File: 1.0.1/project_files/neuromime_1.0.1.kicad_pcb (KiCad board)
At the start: 2 copper layers, 56 x 56 mm, 57 parts, among them K1 inhibit, K2 excite, K3 excite, K4 excite, P1 mnt, P2 axon, P3 axon, P4 axon, P5 long, U1 LM311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

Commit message: work on 1.0.1 board; autoroute test
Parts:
- removed C2, C3: 0.1uF, Capacitor_THT:C_Disc_D3.0mm_W1.6mm_P2.50mm
- moved C1 56.2 mm to (145.1, 69.2)
- moved D5 42.5 mm to (130.9, 60.2), turned to 180 degrees
- moved W3 33.2 mm to (135.4, 60.2)
- moved R8 7.59 mm to (158.3, 36.9), turned to 0 degrees
- moved R10 5.43 mm to (165.4, 63.2)
- moved R12 4.93 mm to (157.0, 63.2)
- moved C11 3.73 mm to (135.9, 67.4)
- moved W1 2.70 mm to (158.3, 27.1), turned to 68 degrees
- moved R15 2.29 mm to (172.0, 46.8), turned to 180 degrees
- moved R13 2.27 mm to (138.2, 70.1)
- moved R9 2.13 mm to (171.7, 43.6)
- moved R5 2.07 mm to (133.6, 37.6), turned to 270 degrees
- moved C10 1.91 mm to (160.0, 62.8)
- moved R11 1.78 mm to (141.9, 70.9)
- moved R7 1.72 mm to (163.8, 34.3), turned to 270 degrees
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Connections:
- C14 pad 1: GND -> Net-(C14-Pad1)
- C14 pad 2: Net-(C14-Pad2) -> GND
- R14 pad 1: Net-(C14-Pad2) -> Net-(C14-Pad1)
- U3 pad 6: Net-(C14-Pad2) -> Net-(C14-Pad1)
- U3 pad 7: Net-(C14-Pad2) -> Net-(C14-Pad1)
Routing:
- net VCC: track 0.00 -> 231.1 mm
- net GND: track 0.00 -> 220.7 mm
- net refractory: track 0.00 -> 76.2 mm
- net Net-(P2-Pad2): track 0.00 -> 60.7 mm
- net Net-(C10-Pad2): track 0.00 -> 51.6 mm
- net Net-(C5-Pad1): track 0.00 -> 43.0 mm
- net Net-(P5-Pad2): track 0.00 -> 23.6 mm
- net Net-(D2-Pad1): track 0.00 -> 18.6 mm
- net Net-(D3-Pad1): track 0.00 -> 18.4 mm
- net Net-(C8-Pad1): track 0.00 -> 15.2 mm
- net Net-(C14-Pad1): track 0.00 -> 13.9 mm
- net Net-(C11-Pad1): track 0.00 -> 13.4 mm
- net Net-(C10-Pad1): track 0.00 -> 12.0 mm
- net Net-(C6-Pad2): track 0.00 -> 11.4 mm
- net Net-(C17-Pad1): track 0.00 -> 11.1 mm
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
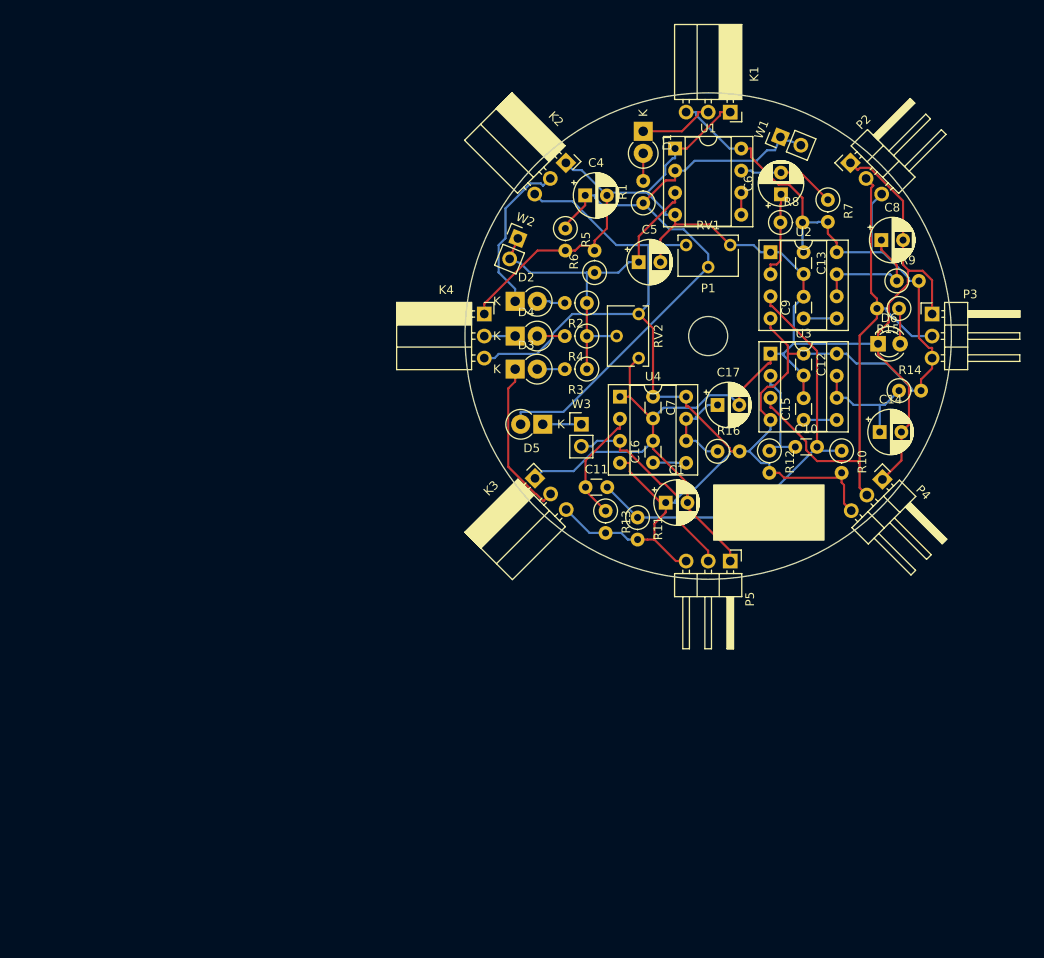
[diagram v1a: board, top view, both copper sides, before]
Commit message: work on 1.0.1; increase autoroute spacing to .5mm; labelling
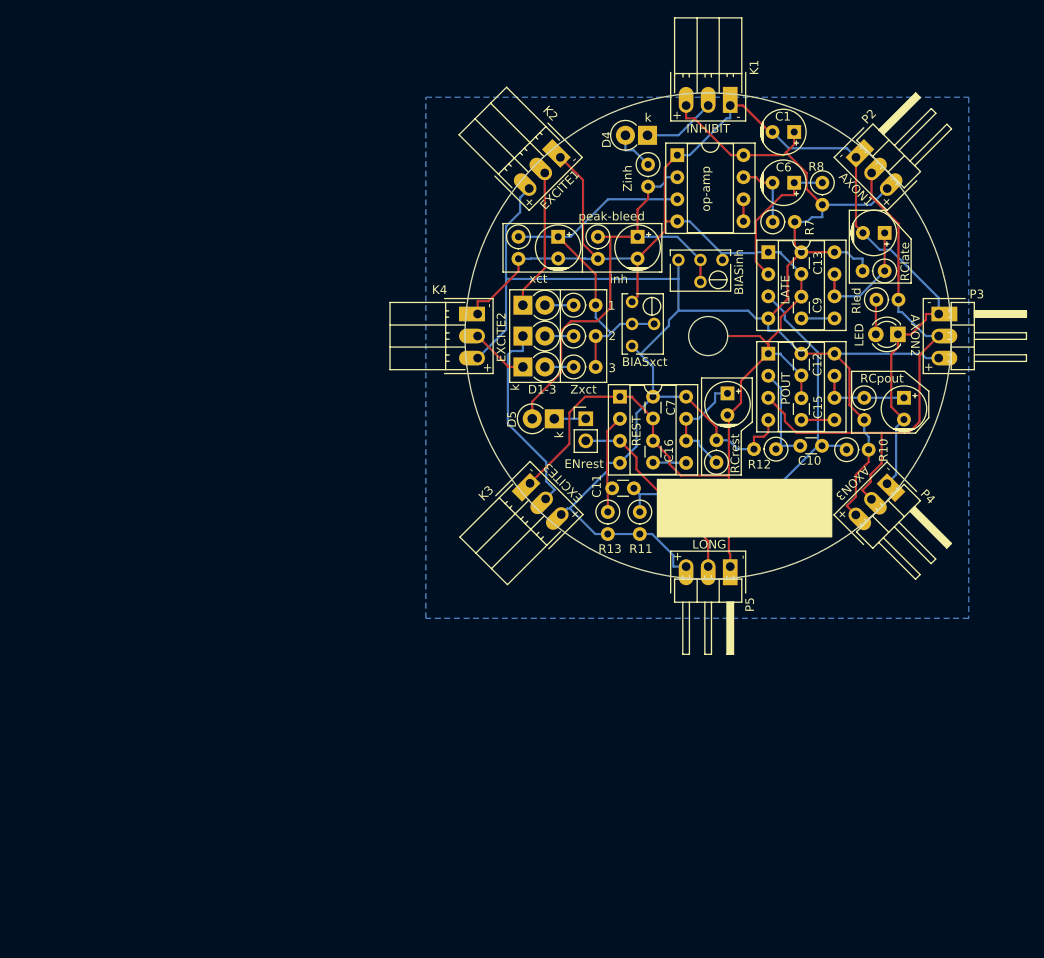
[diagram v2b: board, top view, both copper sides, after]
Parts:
- removed W1: TSTinh, Connector_PinHeader_2.54mm:PinHeader_1x02_P2.54mm_Vertical
- removed W2: TSTxct, Connector_PinHeader_2.54mm:PinHeader_1x02_P2.54mm_Vertical
- C1, C14, C17, C4, C5, C6, C8: footprint Capacitor_THT:CP_Radial_D5.0mm_P2.50mm -> flemming_feetprint_2016:CP_Radial_D5.0mm_P2.50mm_positive_symbol_inside
- K1, K2, K3, K4: footprint Connector_PinSocket_2.54mm:PinSocket_1x03_P2.54mm_Horizontal -> flemming_feetprint_2016:PinSocket_1x03_P2.54mm_Horizontal_elongated
- P2, P3, P4, P5: footprint Connector_PinHeader_2.54mm:PinHeader_1x03_P2.54mm_Horizontal -> flemming_feetprint_2016:PinHeader_1x03_P2.54mm_Horizontal_elomgated_pads
- R1: value Zinh -> Zxct; footprint Resistor_THT:R_Axial_DIN0207_L6.3mm_D2.5mm_P2.54mm_Vertical -> flemming_feetprint_2016:R_Axial_DIN0207_L6.3mm_D2.5mm_P2.54mm_Vertical_pad_numbers_reversed
- R2, R3: footprint Resistor_THT:R_Axial_DIN0207_L6.3mm_D2.5mm_P2.54mm_Vertical -> flemming_feetprint_2016:R_Axial_DIN0207_L6.3mm_D2.5mm_P2.54mm_Vertical_pad_numbers_reversed
- R4: value Zxct -> Zinh; footprint Resistor_THT:R_Axial_DIN0207_L6.3mm_D2.5mm_P2.54mm_Vertical -> flemming_feetprint_2016:R_Axial_DIN0207_L6.3mm_D2.5mm_P2.54mm_Vertical_pad_numbers_reversed
- RV1, RV2: footprint Potentiometer_THT:Potentiometer_Bourns_3266W_Vertical -> flemming_feetprint_2016:Potentiometer_Bourns_3266W_Vertical_pin_variation
- moved C1 45.2 mm to (159.9, 26.5), turned to 180 degrees
- moved D4 27.7 mm to (143.0, 26.9), turned to 180 degrees
- moved D1 24.3 mm to (128.7, 46.4), turned to 0 degrees
- moved R4 21.0 mm to (143.1, 30.3), turned to 270 degrees
- moved R1 14.2 mm to (134.5, 46.4), turned to 0 degrees
- moved C5 9.72 mm to (132.7, 38.6), turned to 270 degrees
- moved R6 9.69 mm to (128.2, 38.6), turned to 270 degrees
- moved C4 7.69 mm to (141.9, 38.6), turned to 270 degrees
- moved R7 6.84 mm to (157.4, 36.9), turned to 0 degrees
- moved R8 6.65 mm to (163.1, 32.3), turned to 270 degrees
- moved RV2 6.52 mm to (141.2, 46.1), turned to 90 degrees
- moved C14 4.83 mm to (172.5, 57.1), turned to 270 degrees
- moved R2 4.10 mm to (134.5, 50.0), turned to 0 degrees
- moved D2 4.10 mm to (128.7, 50.0)
- moved R14 4.09 mm to (168.0, 57.1), turned to 270 degrees
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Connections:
- K1 pad 2: Net-(D1-Pad1) -> Net-(D4-Pad1)
- K2 pad 2: Net-(D2-Pad1) -> Net-(D1-Pad1)
- K3 pad 2: Net-(D3-Pad1) -> Net-(D2-Pad1)
- K4 pad 2: Net-(D4-Pad1) -> Net-(D3-Pad1)
- R1 pad 1: refractory -> Net-(C5-Pad1)
- R4 pad 1: Net-(C5-Pad1) -> refractory
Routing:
- net refractory: track 76.2 -> 52.3 mm
- net GND: track 220.7 -> 236.7 mm
- net Net-(D3-Pad1): track 18.4 -> 6.72 mm
- net Net-(D1-Pad1): track 8.61 -> 16.3 mm
- net Net-(C6-Pad1): track 10.1 -> 17.0 mm
- net Net-(D4-Pad1): track 3.56 -> 8.41 mm
- net Net-(D2-Pad1): track 18.6 -> 22.9 mm
- net Net-(C14-Pad1): track 13.9 -> 10.5 mm
- net Net-(C6-Pad2): track 11.4 -> 8.12 mm
- net Net-(C17-Pad1): track 11.1 -> 13.9 mm
- net Net-(C10-Pad2): track 51.6 -> 48.9 mm
- net Net-(P2-Pad2): track 60.7 -> 62.9 mm
- net Net-(D4-Pad2): track 3.18 -> 5.01 mm
- net Net-(C11-Pad1): track 13.4 -> 11.8 mm
- net Net-(C5-Pad1): track 43.0 -> 44.5 mm
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- added copper zone on B.Cu, net GND
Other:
- board text added: "1"
- board text added: "2"
- board text added: "3"
- board text added: "AXON1"
- board text added: "AXON2"
- board text added: "AXON3"
- board text added: "BIASinh"
- board text added: "BIASxct"
- board text added: "C12"
- board text added: "C13"
- board text added: "C15"
- board text added: "C16"
- board text added: "C7"
- board text added: "C9"
- board text added: "D1-3"
- board text added: "ENrest"
- board text added: "EXCITE1"
- board text added: "EXCITE2"
- board text added: "EXCITE3"
- board text added: "INHIBIT"
- board text added: "LATE"
- board text added: "LED"
- board text added: "LONG"
- board text added: "Norman White's Neuromime version 1.0.1 July 2019, Berlin github.com/gnimm/neuromime"
- board text added: "POUT"
- board text added: "RClate"
- board text added: "RCpout"
- board text added: "RCrest"
- board text added: "REST"
- board text added: "Rled"
- board text added: "Zinh"
- board text added: "Zxct"
- board text added: "inh"
- board text added: "k"
- board text added: "op-amp"
- board text added: "peak-bleed"
- board text added: "xct"

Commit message: work on 1.0.1;housekeeping; paths; included footprints libs
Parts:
- P1: footprint MountingHole:MountingHole_4.5mm -> flemming_feetprint_2019:MountingHole_4.5mm_PTH
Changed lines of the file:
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@@
   (page A4)
   (layers
-    (0 F.Cu signal hide)
+    (0 F.Cu signal)
     (31 B.Cu signal hide)
-    (32 B.Adhes user)
+    (32 B.Adhes user hide)
     (33 F.Adhes user)
-    (34 B.Paste user)
-    (35 F.Paste user)
+    (34 B.Paste user hide)
+    (35 F.Paste user hide)
     (36 B.SilkS user)
     (37 F.SilkS user)
@@
     (46 B.CrtYd user)
     (47 F.CrtYd user)
-    (48 B.Fab user)
+    (48 B.Fab user hide)
     (49 F.Fab user hide)
   )
@@
     )
   )
-  (module MountingHole:MountingHole_4.5mm (layer F.Cu)
-    (at 150 50)
-    (descr "Mounting Hole 4.5mm, no annular")
-    (tags "mounting hole 4.5mm no annular")
-    (attr virtual)
-    (fp_text reference P1 (at 0 -5.5) (layer F.SilkS) hide
-      (effects (font (size 1 1) (thickness 0.15)))
-    )
-    (fp_text value mnt (at 0 5.5) (layer F.Fab) hide
-      (effects (font (size 1 1) (thickness 0.15)))
-    )
-    (fp_circle (center 0 0) (end 4.75 0) (layer F.CrtYd) (width 0.05))
-    (fp_circle (center 0 0) (end 4.5 0) (layer Cmts.User) (width 0.15))
-    (fp_text user %R (at 0.3 0) (layer F.Fab)
-      (effects (font (size 1 1) (thickness 0.15)))
-    )
-    (pad 1 np_thru_hole circle (at 0 0) (size 4.5 4.5) (drill 4.5) (layers *.Cu *.Mask)
-      (net 1 GND))
-  )
   (module Resistor_THT:R_Axial_DIN0207_L6.3mm_D2.5mm_P2.54mm_Vertical (layer F.Cu)
     (at 150.952 64.5415 90)
@@
     )
   )
+  (module flemming_feetprint_2019:MountingHole_4.5mm_PTH (layer F.Cu)
+    (at 150 50)
+    (descr "Mounting Hole 4.5mm, no annular")
+    (tags "mounting hole 4.5mm no annular")
+    (attr virtual)
+    (fp_text reference P1 (at 0 -5.5) (layer F.SilkS) hide
+      (effects (font (size 1 1) (thickness 0.15)))
+    )
+    (fp_text value mnt (at 0 5.5) (layer F.Fab) hide
+      (effects (font (size 1 1) (thickness 0.15)))
+    )
+    (fp_circle (center 0 0) (end 4.75 0) (layer F.CrtYd) (width 0.05))
+    (fp_circle (center 0 0) (end 4.5 0) (layer Cmts.User) (width 0.15))
+    (fp_text user %R (at 0.3 0) (layer F.Fab)
+      (effects (font (size 1 1) (thickness 0.15)))
+    )
+    (pad 1 thru_hole circle (at 0 0) (size 4.5 4.5) (drill 4.5) (layers *.Cu *.Mask)
+      (net 1 GND))
+  )
   (gr_text "Norman White's Neuromime\nversion 1.0.1\nJuly 2019, Berlin\ngithub.com/gnimm/neuromime\n" (at 165.367 69.05) (layer B.SilkS)
